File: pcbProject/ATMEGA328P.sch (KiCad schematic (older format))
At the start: 10 parts, among them SW1 RESET_SWITCH, U2 ATmega328P-AU, Y1 CSTCE16MOV53-R0

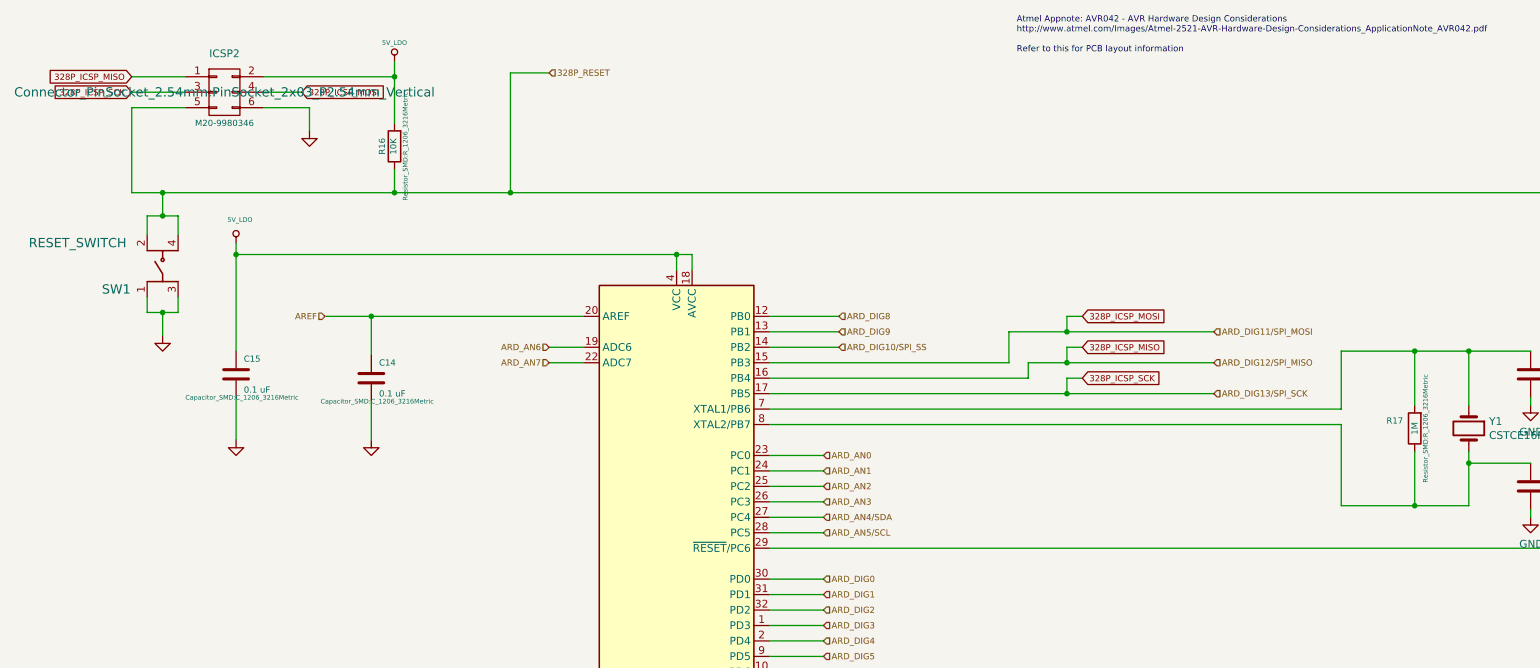
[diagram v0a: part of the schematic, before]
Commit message: PCB versie3
Aanpassingen tips coach --> veel gewijzigd
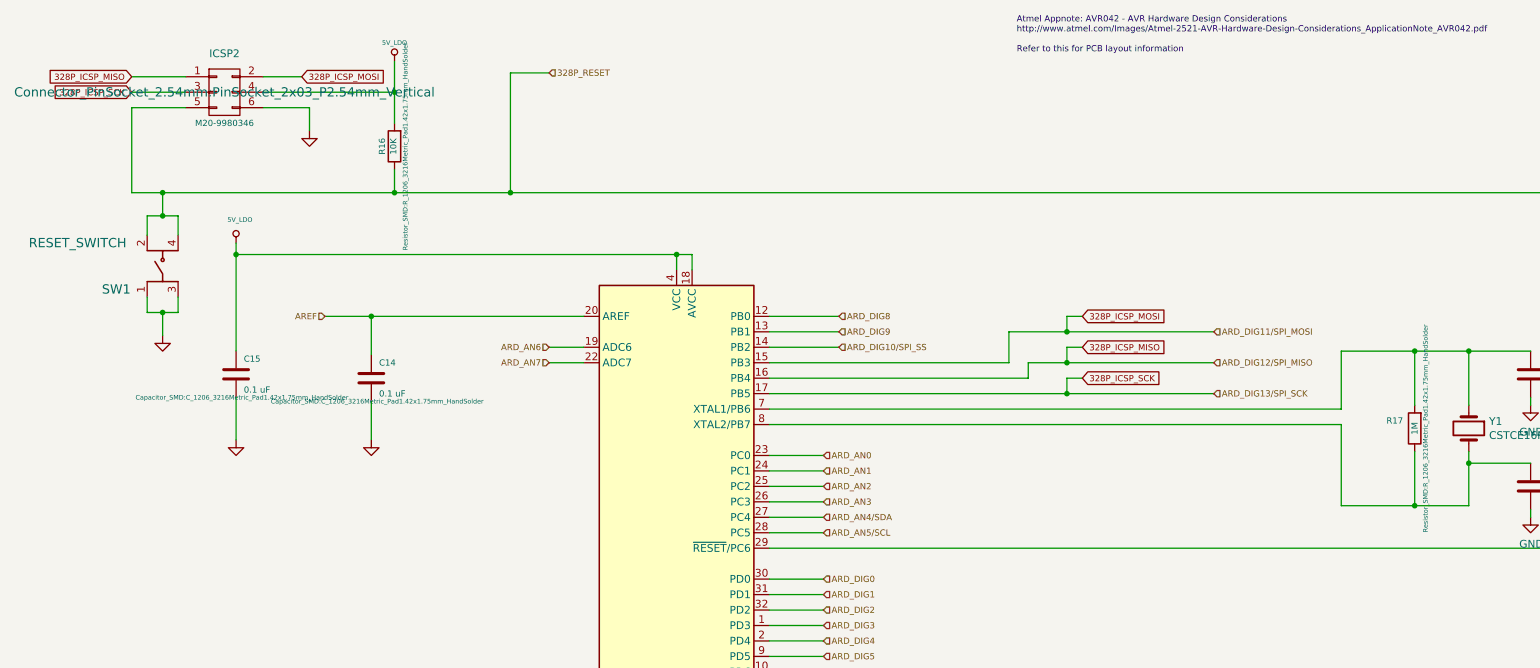
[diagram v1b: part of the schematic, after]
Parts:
- C14, C15: footprint Capacitor_SMD:C_1206_3216Metric -> Capacitor_SMD:C_1206_3216Metric_Pad1.42x1.75mm_HandSolder
- C19, C20: footprint Capacitor_SMD:C_0805_2012Metric -> Capacitor_SMD:C_0805_2012Metric_Pad1.15x1.40mm_HandSolder
- R16, R17: footprint Resistor_SMD:R_1206_3216Metric -> Resistor_SMD:R_1206_3216Metric_Pad1.42x1.75mm_HandSolder
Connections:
- net 328P_ICSP_MOSI: now also ICSP2.2 (P2); no longer ICSP2.4 (P4)
- net 5V_LDO: now also ICSP2.4 (P4); no longer ICSP2.2 (P2)
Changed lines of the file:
@@
 $EndComp
-Wire Wire Line
-	3000 1100 3000 1200
 Wire Wire Line
 	3000 1800 3000 1950
-Connection ~ 3000 1200
-Wire Wire Line
-	2150 1200 3000 1200
 Wire Wire Line
 	2450 1400 2450 1550
@@
 Text GLabel 1300 1200 0    40   Input ~ 0
 328P_ICSP_MISO
-Text GLabel 2400 1300 2    40   Input ~ 0
+Text GLabel 2400 1200 2    40   Input ~ 0
 328P_ICSP_MOSI
-Wire Wire Line
-	2150 1300 2400 1300
 $Comp
 L Arduino_Uno_R3_From_Scratch:RESET_SWITCH SW1
@@
 F 0 "C14" H 2900 3250 40  0000 L CNN
 F 1 "0.1 uF" H 2900 3050 40  0000 L CNN
-F 2 "Capacitor_SMD:C_1206_3216Metric" H 2888 3000 30  0000 C CNN
+F 2 "Capacitor_SMD:C_1206_3216Metric_Pad1.42x1.75mm_HandSolder" H 2888 3000 30  0000 C CNN
 F 3 "http://images.ihscontent.net/vipimages/VipMasterIC/IC/KEME/KEMES10043/KEMES10043-1.pdf" H 2850 3150 60  0001 C CNN
 F 4 "CAPACITOR, CERAMIC, MULTILAYER, 100 V, X7R, 0.1 uF, SURFACE MOUNT, 0805, CHIP, ROHS COMPLIANT" H 2850 3150 60  0001 C CNN "Characteristics"
@@
 F 0 "C15" H 2025 3225 40  0000 L CNN
 F 1 "0.1 uF" H 2025 3025 40  0000 L CNN
-F 2 "Capacitor_SMD:C_1206_3216Metric" H 2013 2975 30  0000 C CNN
+F 2 "Capacitor_SMD:C_1206_3216Metric_Pad1.42x1.75mm_HandSolder" H 2013 2975 30  0000 C CNN
 F 3 "http://images.ihscontent.net/vipimages/VipMasterIC/IC/KEME/KEMES10043/KEMES10043-1.pdf" H 1975 3125 60  0001 C CNN
 F 4 "CAPACITOR, CERAMIC, MULTILAYER, 100 V, X7R, 0.1 uF, SURFACE MOUNT, 0805, CHIP, ROHS COMPLIANT" H 1975 3125 60  0001 C CNN "Characteristics"
@@
 F 0 "R16" V 3080 1650 40  0000 C CNN
 F 1 "10K" V 3007 1651 40  0000 C CNN
-F 2 "Resistor_SMD:R_1206_3216Metric" V 2930 1650 30  0000 C CNN
+F 2 "Resistor_SMD:R_1206_3216Metric_Pad1.42x1.75mm_HandSolder" V 2930 1650 30  0000 C CNN
 F 3 "http://images.ihscontent.net/vipimages/VipMasterIC/IC/VISH/VISHS75859/VISHS75859-1.pdf" H 3000 1650 30  0001 C CNN
 F 4 "RESISTOR, METAL GLAZE/THICK FILM, 0.125W, 5%, 200ppm, 10000ohm, SURFACE MOUNT, 0805" H 3000 1650 60  0001 C CNN "Characteristics"
@@
 F 0 "R17" H 9675 3425 40  0000 L CNN
 F 1 "1M" V 9600 3475 40  0000 C CNN
-F 2 "Resistor_SMD:R_1206_3216Metric" V 9530 3475 30  0000 C CNN
+F 2 "Resistor_SMD:R_1206_3216Metric_Pad1.42x1.75mm_HandSolder" V 9530 3475 30  0000 C CNN
 F 3 "http://www.vishay.com/docs/20035/dcrcwe3.pdf" H 9600 3475 30  0001 C CNN
 F 4 "RES SMD 1M OHM 1% 1/8W 0805" H 9600 3475 60  0001 C CNN "Characteristics"
@@
 $EndComp
 Wire Wire Line
-	3000 1200 3000 1500
-Wire Wire Line
 	7350 3250 8300 3250
 Wire Wire Line
@@
 F 0 "C20" H 10465 3896 50  0000 L CNN
 F 1 "22p" H 10465 3805 50  0000 L CNN
-F 2 "Capacitor_SMD:C_0805_2012Metric" H 10388 3700 50  0001 C CNN
+F 2 "Capacitor_SMD:C_0805_2012Metric_Pad1.15x1.40mm_HandSolder" H 10388 3700 50  0001 C CNN
 F 3 "~" H 10350 3850 50  0001 C CNN
 	1    10350 3850
@@
 F 0 "C19" H 10465 3171 50  0000 L CNN
 F 1 "22p" H 10465 3080 50  0000 L CNN
-F 2 "Capacitor_SMD:C_0805_2012Metric" H 10388 2975 50  0001 C CNN
+F 2 "Capacitor_SMD:C_0805_2012Metric_Pad1.15x1.40mm_HandSolder" H 10388 2975 50  0001 C CNN
 F 3 "~" H 10350 3125 50  0001 C CNN
 	1    10350 3125
@@
 Wire Wire Line
 	10350 4050 10350 4000
+Wire Wire Line
+	3000 1100 3000 1300
+Wire Wire Line
+	2400 1200 2150 1200
+Wire Wire Line
+	2150 1300 3000 1300
+Connection ~ 3000 1300
+Wire Wire Line
+	3000 1300 3000 1500
 $EndSCHEMATC

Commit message: verslag
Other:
- moved on the sheet: C14, C15, C19, C20, ICSP2, R16, R17, SW1, Y1
